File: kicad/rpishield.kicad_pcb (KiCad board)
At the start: 2 copper layers, 64 x 55 mm, 23 parts

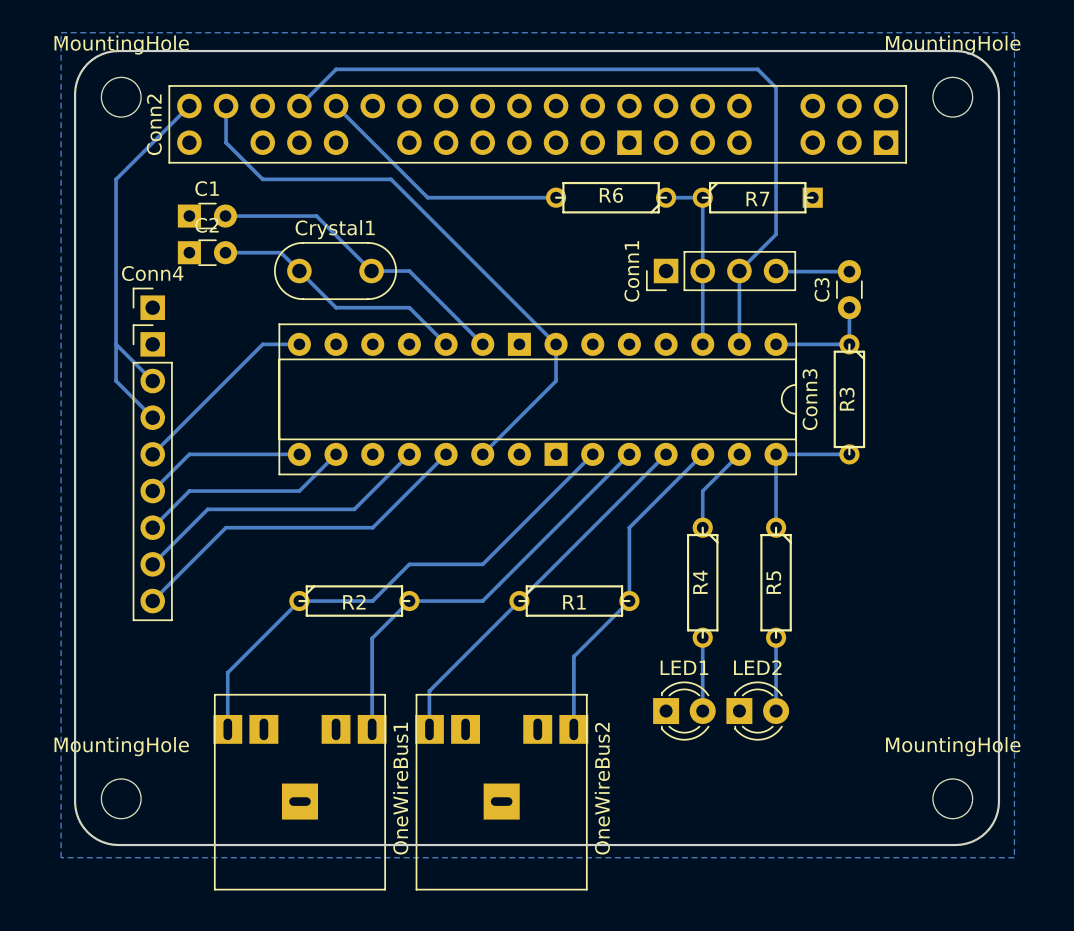
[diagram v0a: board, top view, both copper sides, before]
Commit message: Mounthole,Jack,Crystal PCB fix.
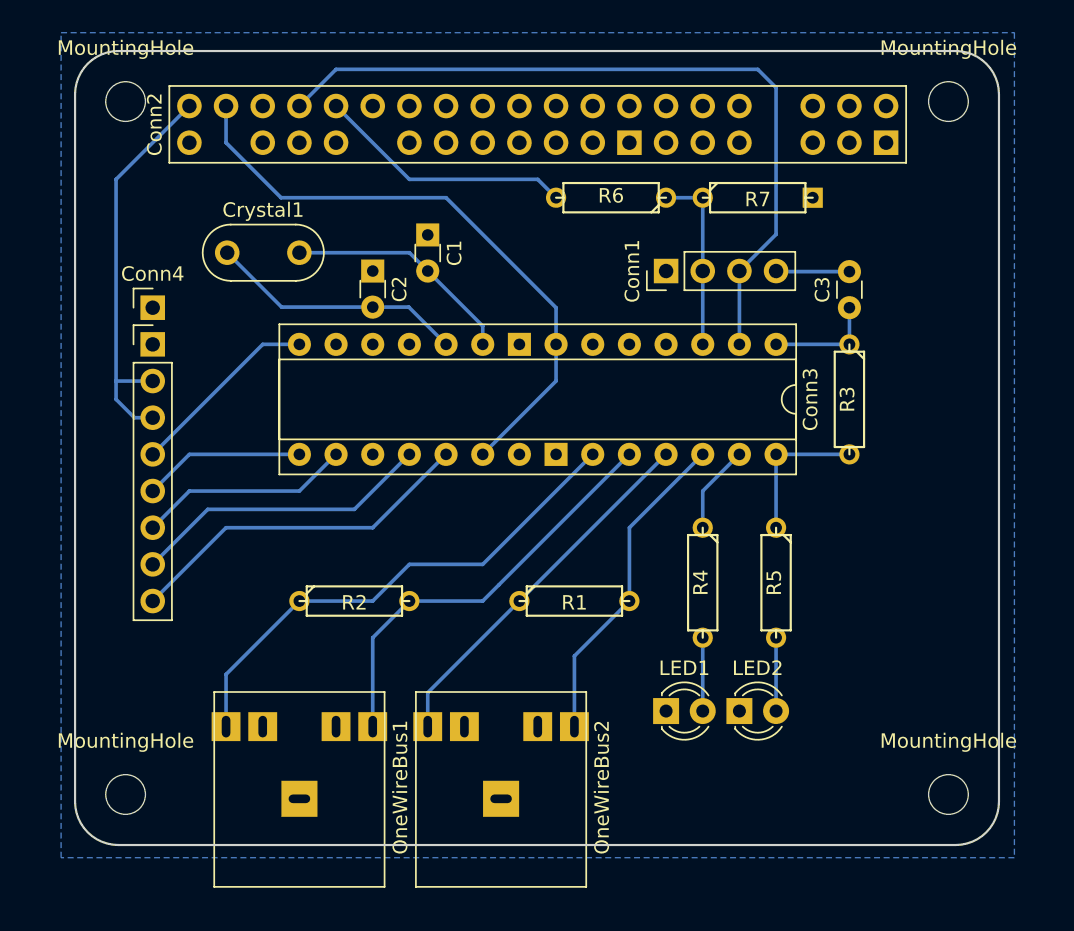
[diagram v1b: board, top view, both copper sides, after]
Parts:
- MountingHole (x4): footprint Mounting_Holes:MountingHole_2.7mm_M2.5 -> footprint:Custom_MountingHole_2.75mm_M2.5
- moved C1 16.6 mm to (138.4, 76.2), turned to 270 degrees
- moved C2 12.8 mm to (134.6, 78.7), turned to 270 degrees
- moved OneWireBus1 6.04 mm to (129.5, 121.5)
- moved OneWireBus2 6.04 mm to (143.5, 121.5)
- moved Crystal1 5.16 mm to (124.5, 77.5)
- moved MountingHole 0.42 mm to (174.5, 67.0)
- moved MountingHole 0.42 mm to (174.5, 115.0)
- moved MountingHole 0.42 mm to (117.5, 115.0)
- moved MountingHole 0.42 mm to (117.5, 67.0)
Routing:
- net /XTAL1: track 21.5 -> 16.1 mm
- net /VCC_ADC: track 40.9 -> 42.4 mm

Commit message: Board,LED,AVR spacing.
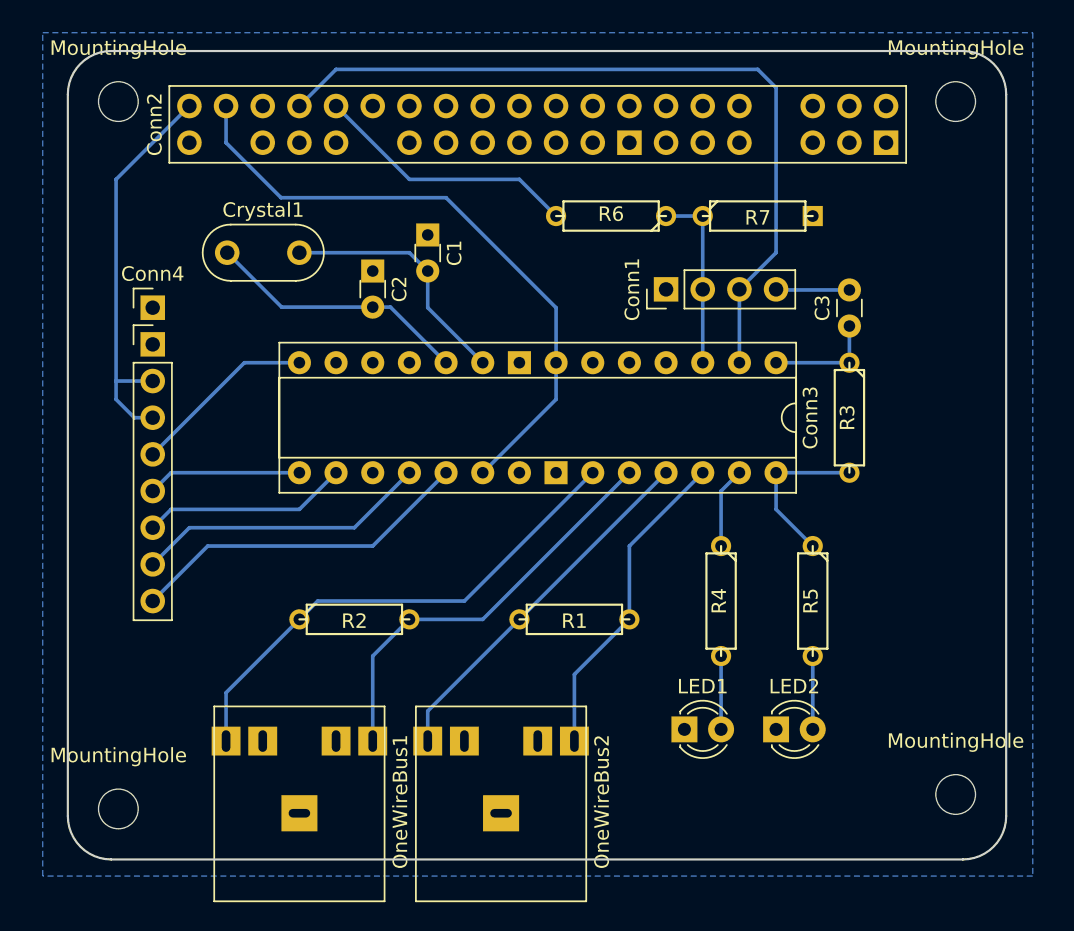
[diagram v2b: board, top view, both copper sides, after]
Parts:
- moved LED2 2.84 mm to (162.6, 110.5)
- moved R5 2.84 mm to (165.1, 101.6)
- moved LED1 1.80 mm to (156.2, 110.5)
- moved R4 1.80 mm to (158.8, 101.6)
- moved Conn1 1.27 mm to (154.9, 80.0)
- moved Conn3 1.27 mm to (162.6, 85.1)
- moved R1 1.27 mm to (148.6, 102.9)
- moved R2 1.27 mm to (133.3, 102.9)
- moved R3 1.27 mm to (167.6, 88.9)
- moved R6 1.27 mm to (151.1, 74.9)
- moved R7 1.27 mm to (161.3, 74.9)
- moved C3 1.27 mm to (167.6, 82.5)
- moved MountingHole 1.12 mm to (117.0, 116.0)
- moved OneWireBus1 1.00 mm to (129.5, 122.5)
- moved OneWireBus2 1.00 mm to (143.5, 122.5)
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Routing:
- net /XTAL1: track 16.1 -> 17.3 mm
- net /RX: track 53.4 -> 54.7 mm
- net /VCC_ADC: track 42.4 -> 43.7 mm
- net /LED_PWR: track 10.2 -> 11.2 mm
- net /TFT_DC: track 13.3 -> 12.8 mm
- net /RX_RPI: track 17.9 -> 18.4 mm
- net /XTAL2: track 17.8 -> 18.3 mm
- net /SPI_SS: track 14.8 -> 14.3 mm
- net /SPI_SCK: track 24.5 -> 24.0 mm
- net /TFT_RST: track 11.2 -> 10.7 mm
- net /SPI_MOSI: track 20.9 -> 20.4 mm
- net /LED_ACC: track 6.13 -> 5.61 mm
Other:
- board size 64 x 55 mm -> 65 x 56 mm

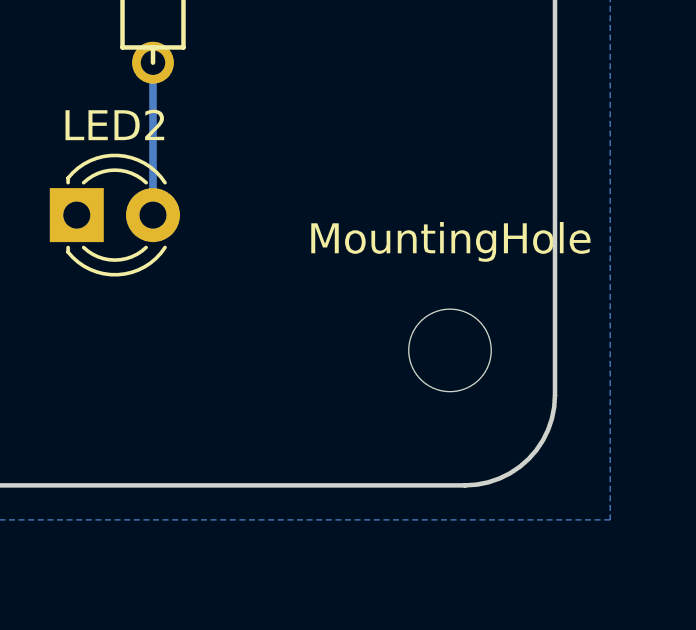
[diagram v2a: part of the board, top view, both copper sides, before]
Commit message: Hole fix.
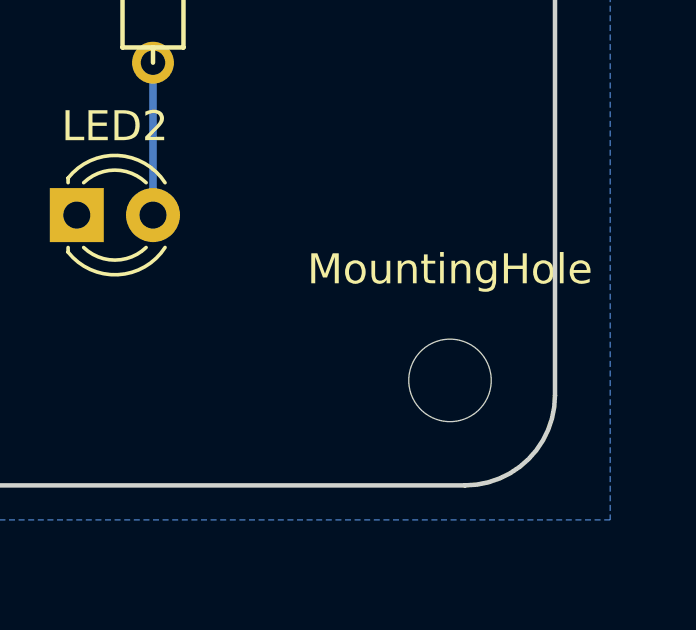
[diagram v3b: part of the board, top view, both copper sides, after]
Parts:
- moved MountingHole 1.00 mm to (175.0, 116.0)
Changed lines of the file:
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@@
   )
   (module footprint:Custom_MountingHole_2.75mm_M2.5 (layer F.Cu)
-    (at 175 115)
+    (at 175 116)
     (descr "Mounting Hole 2.7mm, no annular, M2.5")
     (tags "mounting hole 2.7mm no annular m2.5")

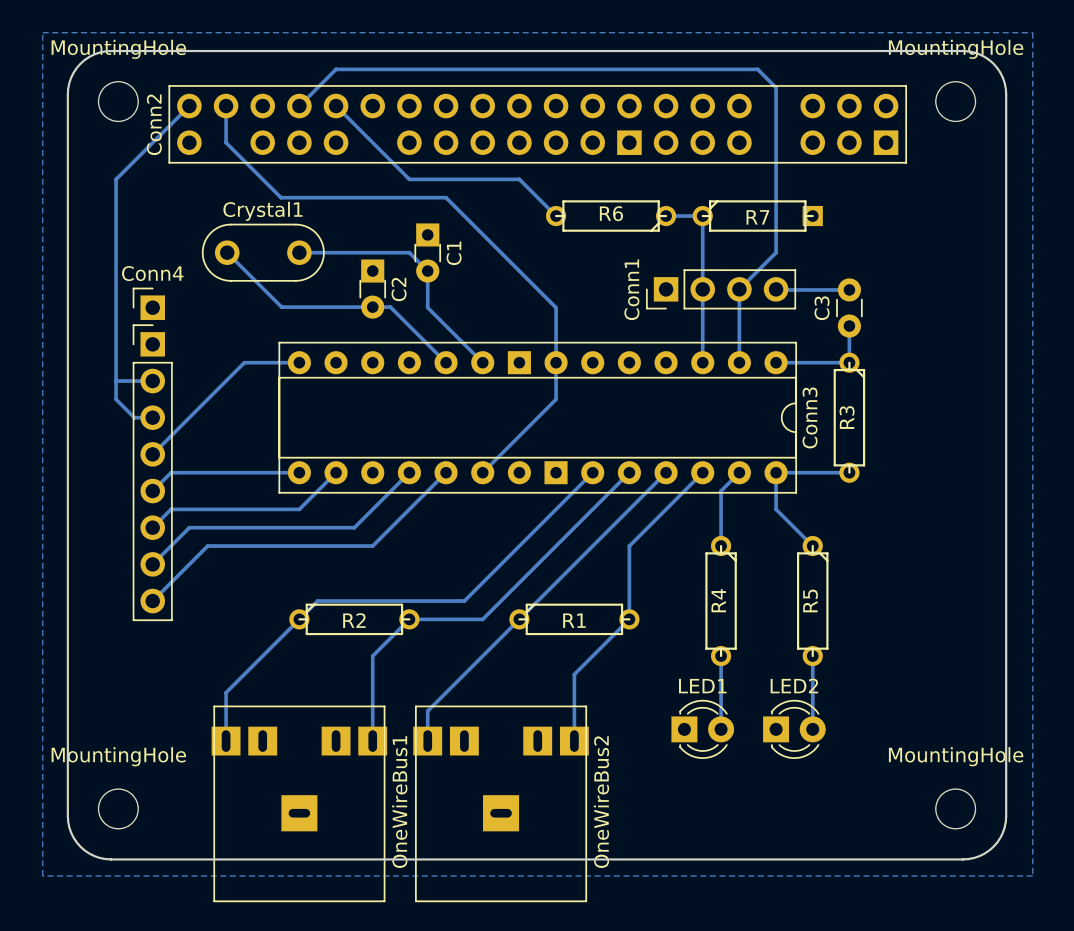
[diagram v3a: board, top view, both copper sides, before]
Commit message: Crystal layout.
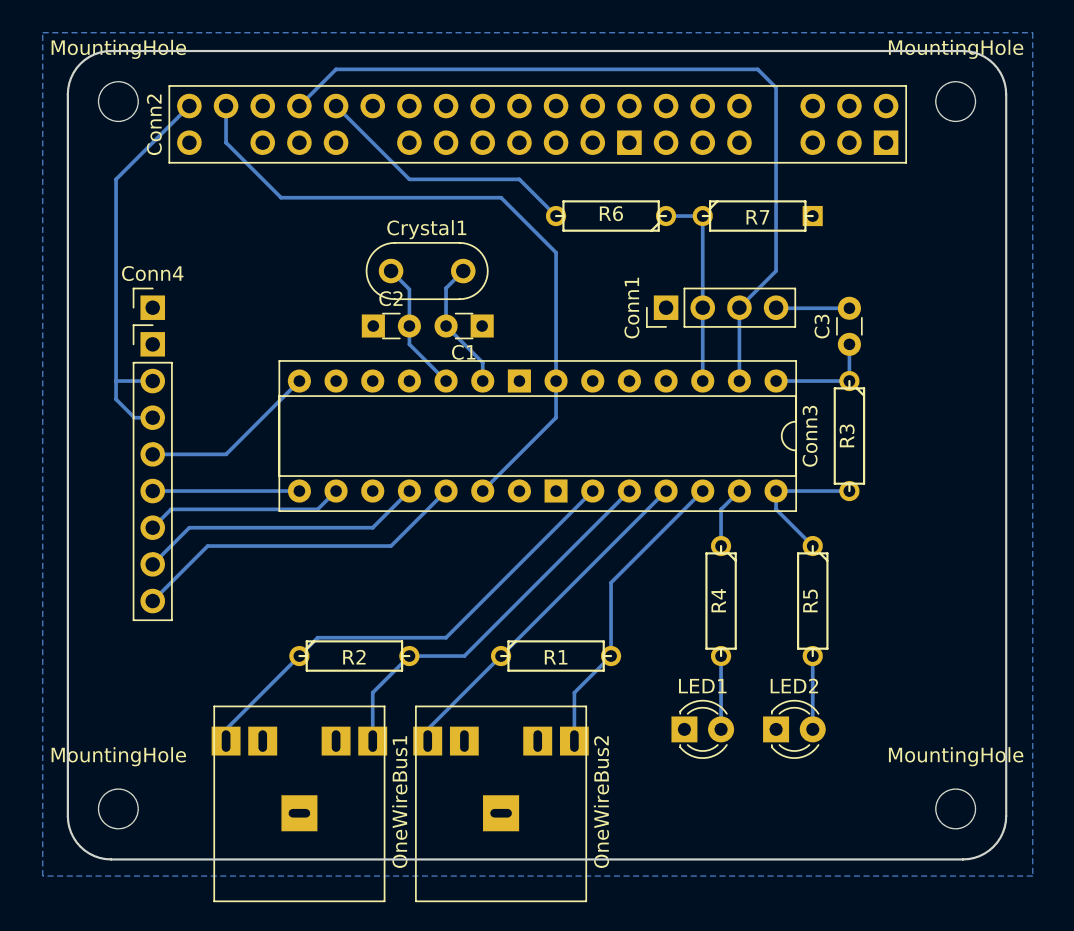
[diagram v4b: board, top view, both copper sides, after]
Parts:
- moved Crystal1 11.4 mm to (135.9, 78.7)
- moved C1 7.35 mm to (142.2, 82.5), turned to 180 degrees
- moved C2 3.81 mm to (134.7, 82.5), turned to 0 degrees
- moved R1 2.84 mm to (147.3, 105.4)
- moved R2 2.54 mm to (133.3, 105.4)
- moved C3 1.27 mm to (167.6, 83.8)
- moved Conn1 1.27 mm to (154.9, 81.3)
- moved Conn3 1.27 mm to (162.6, 86.4)
- moved R3 1.27 mm to (167.6, 90.2)
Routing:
- net /XTAL2: track 18.3 -> 9.20 mm
- net /XTAL1: track 17.3 -> 9.17 mm
- net /VCC_ADC: track 43.7 -> 47.2 mm
- net /BUS1_DQ: track 28.9 -> 26.9 mm
- net /BUS1_PWR: track 35.1 -> 33.0 mm
- net /LED_PWR: track 11.2 -> 9.94 mm
- net /BUS2_PWR: track 25.4 -> 24.2 mm
- net /BUS2_DQ: track 22.3 -> 21.0 mm
- net /LED_ACC: track 5.61 -> 4.34 mm
- net /TX: track 12.7 -> 14.0 mm
- net /RX: track 54.7 -> 56.0 mm
- net /SPI_SCK: track 24.0 -> 23.5 mm
- net /SPI_MOSI: track 20.4 -> 19.9 mm
- net /TFT_RST: track 10.7 -> 10.2 mm
- net /SPI_SS: track 14.3 -> 13.8 mm
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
